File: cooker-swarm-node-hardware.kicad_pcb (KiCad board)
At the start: 2 copper layers, 44.2 x 26.5 mm, 55 parts, among them J1 Conn_ARM_JTAG_SWD_10, J2 Conn_INPUT, J3 Conn_OUTPUT, J4 USB_B_Micro, Q1 BSS138, Q2 BSS138, U1 nRF52840, U2 MCP6002-xMC, X1 32MHz, 8pF, X2 32,768kHz, 9pF

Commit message: use different footprint for operational amplifier
makes soldering more easier
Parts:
- J3: footprint Connector_PinHeader_2.54mm:PinHeader_1x10_P2.54mm_Vertical -> Connector_PinSocket_2.54mm:PinSocket_1x10_P2.54mm_Vertical
- U2: value MCP6002-xMC -> MCP6002-xMS; footprint Package_DFN_QFN:DFN-8-1EP_3x2mm_P0.5mm_EP1.75x1.45mm -> Package_SO:MSOP-8_3x3mm_P0.65mm
- moved R7 1.93 mm to (140.9, 104.6)
- moved R9 1.93 mm to (139.9, 104.6)
- moved C25 1.32 mm to (139.4, 101.4), turned to 180 degrees
- moved R3 1.05 mm to (140.4, 102.7), turned to 180 degrees
- moved R11 1.04 mm to (135.0, 101.6)
- moved U2 0.85 mm to (136.2, 103.9)
- moved R12 0.79 mm to (136.9, 101.6)
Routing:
- net Net-(R3-Pad1): track 18.3 -> 21.0 mm
- net /POWER_OUT: track 8.45 -> 10.3 mm
- net /LV_POWER_IN: track 20.4 -> 19.1 mm
- net GND: track 53.0 -> 52.0 mm, vias 27 -> 26
- net +5V: track 63.7 -> 62.9 mm
- net /POWER_IN: track 7.39 -> 7.02 mm, vias 1 -> 0
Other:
- board text added: "cooker-swarm-node-hardware-v1.0.1"
- board text removed: "cooker-swarm-node-hardware-v1.0.0"

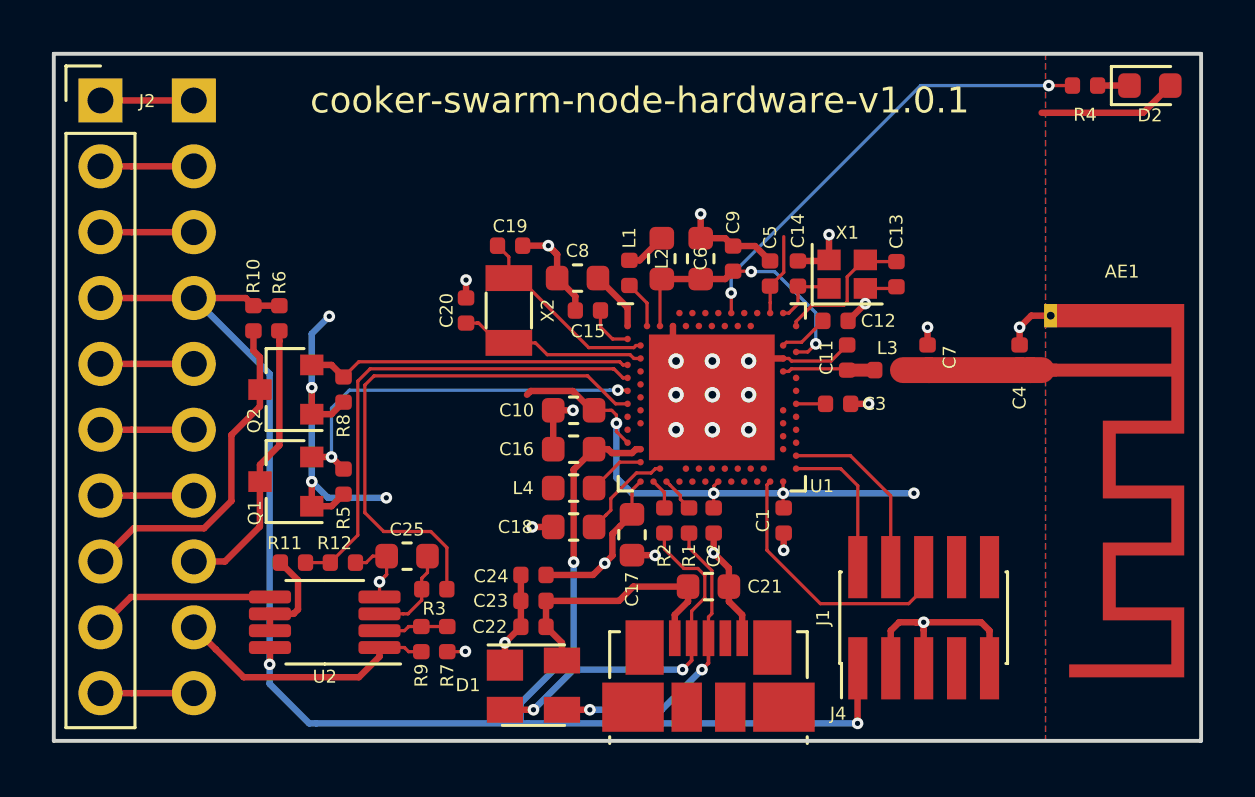
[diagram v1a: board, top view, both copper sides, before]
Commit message: use MCP6002 opamp
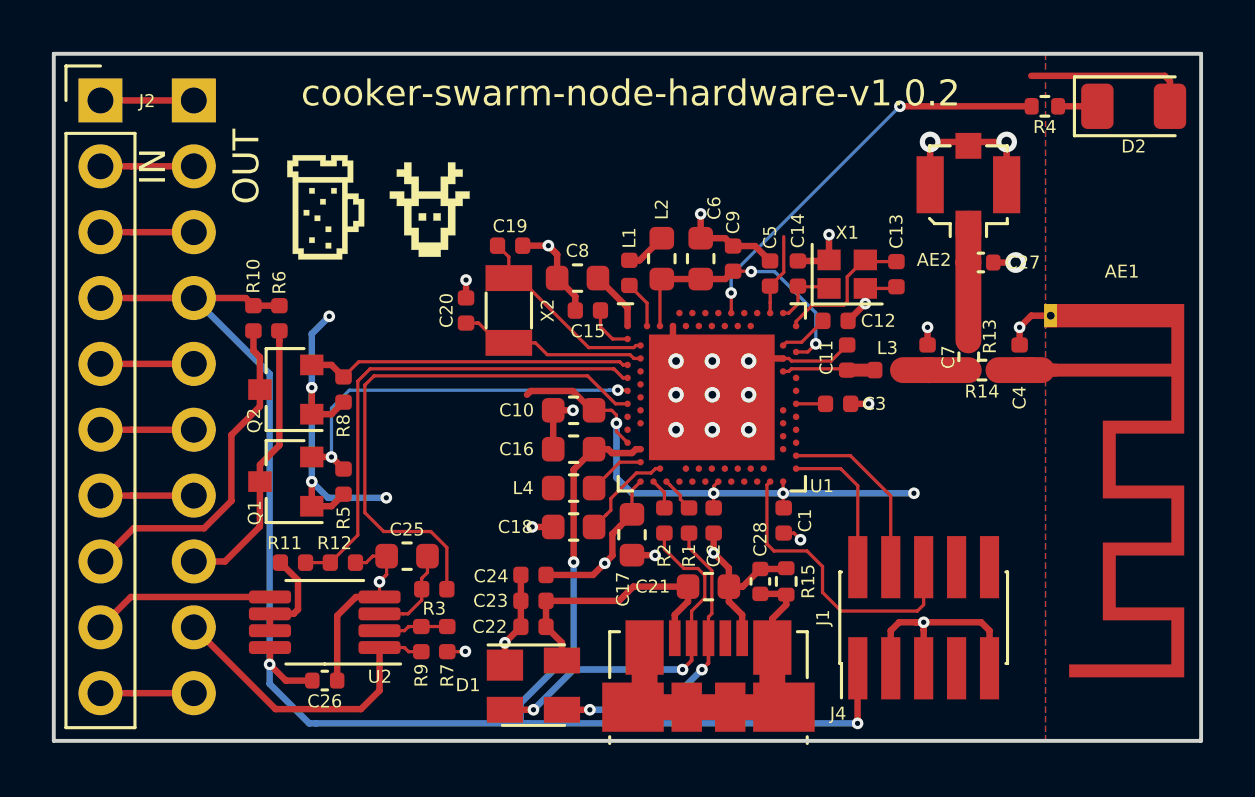
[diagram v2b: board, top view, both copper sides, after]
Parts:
- removed the G*** at (150.7, 95.3)
- added AE2: Antenna_Shield, Connector_Coaxial:U.FL_Molex_MCRF_73412-0110_Vertical, F.Cu at (161.0, 87.0)
- added C26: 10n, Capacitor_SMD:C_0402_1005Metric, F.Cu at (136.2, 106.2)
- added C27: N.C., Capacitor_SMD:C_0402_1005Metric, F.Cu at (161.5, 90.0)
- added C28: 100n, Capacitor_SMD:C_0402_1005Metric, F.Cu at (153.0, 102.3)
- added G***: LOGO, Misc:brewce_logo_1200, F.Cu at (136.0, 88.0)
- added G***: LOGO, Misc:didee_logo_4.9x4, F.Cu at (140.2, 88.0)
- added R13: 0, Resistor_SMD:R_0402_1005Metric, F.Cu at (161.0, 93.7)
- added R14: 0, Resistor_SMD:R_0402_1005Metric, F.Cu at (161.6, 94.2)
- added R15: 10k, Resistor_SMD:R_0402_1005Metric, F.Cu at (154.0, 102.3)
- D2: footprint LED_SMD:LED_0603_1608Metric -> LED_SMD:LED_1206_3216Metric
- R10: value 10k -> 10k (N.C.)
- moved R4 1.74 mm to (164.0, 84.0)
- moved D2 1.02 mm to (167.4, 84.0)
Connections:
- C7 pad 1: Net-(AE1-Pad1) -> Net-(C7-Pad1)
- L3 pad 1: Net-(AE1-Pad1) -> Net-(C7-Pad1)
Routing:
- net GND: track 52.0 -> 66.3 mm, vias 26 -> 29
- net Net-(C28-Pad1): track 0.00 -> 14.1 mm
- net Net-(AE2-Pad1): track 0.00 -> 4.50 mm
- net Net-(AE1-Pad1): track 5.35 -> 1.67 mm
- net Net-(C7-Pad1): track 0.00 -> 2.59 mm
- net /LED: track 17.7 -> 15.8 mm
- net +5V: track 62.9 -> 64.8 mm
- net /POWER_OUT: track 10.3 -> 12.1 mm
- net /SWO: track 10.7 -> 11.7 mm
- net VCC: track 46.6 -> 47.6 mm
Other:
- board text added: "IN"
- board text added: "OUT"
- board text added: "cooker-swarm-node-hardware-v1.0.2"
- board text removed: "cooker-swarm-node-hardware-v1.0.1"
